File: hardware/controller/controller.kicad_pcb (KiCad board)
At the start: 2 copper layers, 47 parts, among them J1 Conn_01x02_Pin, J11 Barrel_Jack, J12 USB_C_Receptacle_USB2.0_14P, J2 Conn_01x02_Pin, J3 Conn_01x02_Pin, J5 Screw_Terminal_01x02, J6 Screw_Terminal_01x02, J7 Conn_01x04_Pin, J8 Conn_01x04_Pin, U1 ESP32-C3-MINI-1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

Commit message: First stab at board routing
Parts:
- removed C9: 0.1uf, Capacitor_SMD:C_0805_2012Metric
- removed the R4 at (155.4, 96.5)
- J6: moved to F.Cu
- TP1, TP2, TP3, TP4, TP5: footprint TestPoint:TestPoint_Pad_D2.0mm -> TestPoint:TestPoint_THTPad_2.0x2.0mm_Drill1.0mm
- moved TP1 42.5 mm to (121.3, 113.0)
- moved TP2 41.1 mm to (117.5, 113.0)
- moved TP3 40.4 mm to (113.7, 113.0)
- moved R2 23.4 mm to (129.8, 75.6), turned to 90 degrees
- moved R11 22.8 mm to (129.8, 79.4), turned to -90 degrees
- moved R9 18.4 mm to (121.9, 96.3), turned to -90 degrees
- moved TP4 16.5 mm to (158.1, 77.9)
- moved TP5 16.5 mm to (158.1, 81.9)
- moved C2 15.6 mm to (122.6, 104.5), turned to -90 degrees
- moved U8 15.3 mm to (118.5, 92.7)
- moved C8 15.1 mm to (113.5, 74.6), turned to 90 degrees
- moved U9 15.1 mm to (118.5, 96.3)
- moved D2 14.9 mm to (160.2, 104.6)
- moved R8 14.6 mm to (121.9, 92.7), turned to -90 degrees
- moved R3 14.2 mm to (160.1, 106.9)
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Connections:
- U1 pad 18: SCK -> CS0
- U1 pad 19: CS0 -> SCK
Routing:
- net GND: track 0.00 -> 95.5 mm, vias 0 -> 43
- net /Microcontroller/HEATER: track 0.00 -> 82.3 mm, vias 0 -> 2
- net +12V: track 0.00 -> 75.5 mm, vias 0 -> 1
- net SO: track 0.00 -> 49.9 mm
- net SCK: track 0.00 -> 47.5 mm, vias 0 -> 3
- net VBUS: track 0.00 -> 39.3 mm, vias 0 -> 2
- net FAN_1_TACH: track 0.00 -> 36.3 mm
- net FAN_0_TACH: track 0.00 -> 33.3 mm
- net CS2: track 0.00 -> 32.4 mm
- net +3V3: track 0.00 -> 28.7 mm, vias 0 -> 10
- net /Microcontroller/USB_D+: track 0.00 -> 28.0 mm, vias 0 -> 2
- net /Microcontroller/LED: track 0.00 -> 26.7 mm, vias 0 -> 2
- net CS1: track 0.00 -> 26.1 mm
- net CS0: track 0.00 -> 25.8 mm
- net /Microcontroller/USB_D-: track 0.00 -> 25.7 mm, vias 0 -> 2
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- added copper zone on In2.Cu, net +3V3
- added copper zone on F.Cu, net GND
- added copper zone on In1.Cu, net GND
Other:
- board outline added: 57.9 x 45.2 mm
- copper layers 2 -> 4
- board text added: "Andrew Reilley v1"
- board text added: "EZ-Bake"

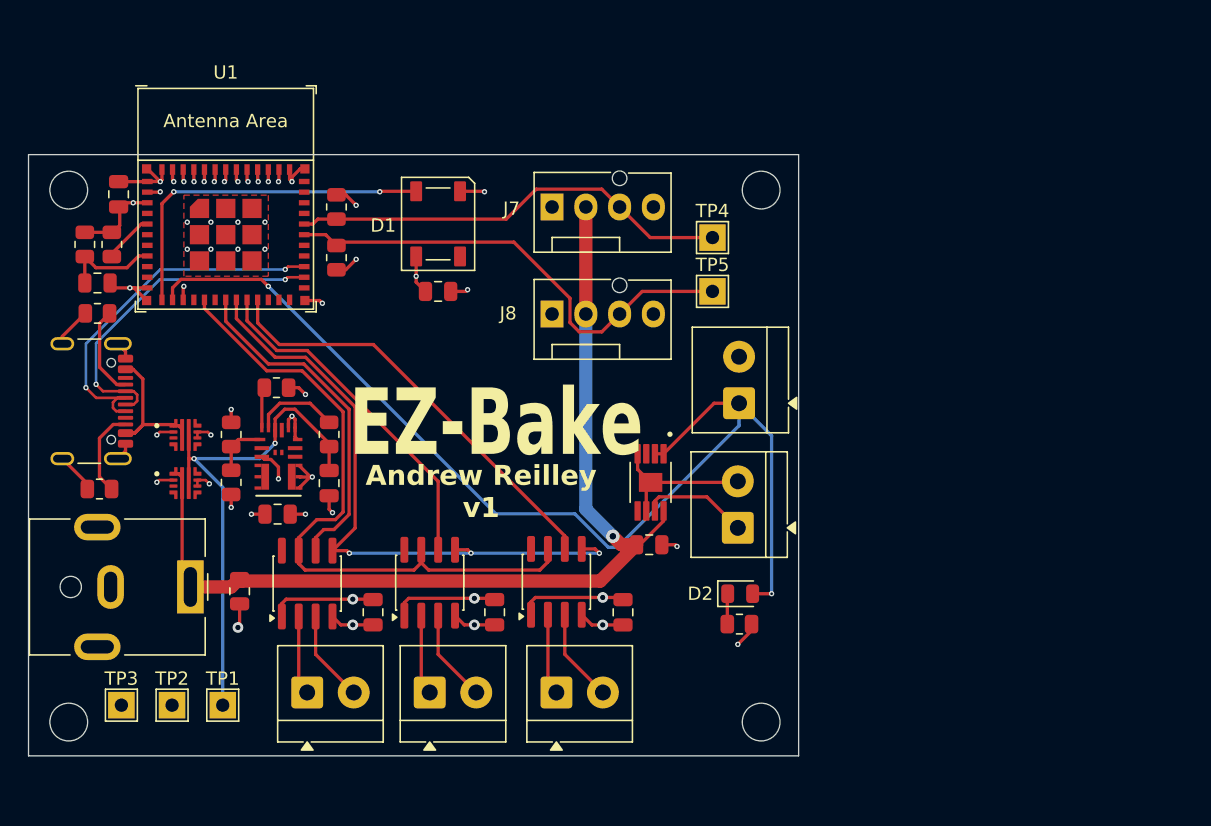
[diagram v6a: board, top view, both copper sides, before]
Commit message: Layout tweaks
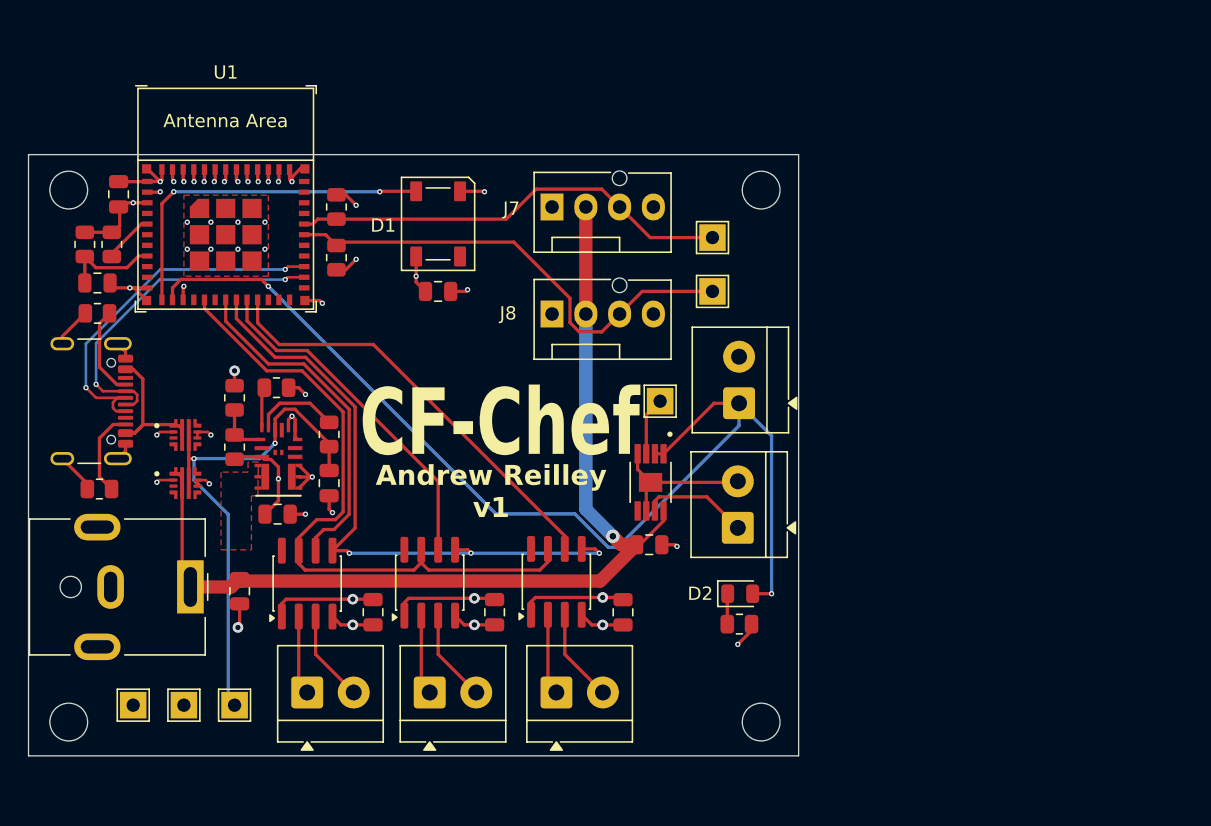
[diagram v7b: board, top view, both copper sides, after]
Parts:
- added TP6: TestPoint, TestPoint:TestPoint_THTPad_2.0x2.0mm_Drill1.0mm, F.Cu at (154.2, 90.2)
- moved R8 2.77 mm to (122.2, 89.9)
- moved R9 2.67 mm to (122.2, 93.6)
- moved TP1 0.89 mm to (122.2, 113.0)
- moved TP2 0.89 mm to (118.4, 113.0)
- moved TP3 0.89 mm to (114.6, 113.0)
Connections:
- U6 pad 3: unconnected-(U6-~{FAULT}-Pad3) -> Net-(U6-~{FAULT})
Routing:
- net Net-(U6-~{FAULT}): track 0.00 -> 4.39 mm
- net GND: track 95.5 -> 98.7 mm, vias 43 -> 41
- added copper zone on F.Cu, net /Power/V_SW
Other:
- board text added: "${REFERENCE}"
- board text added: "CF-Chef"
- board text removed: "EZ-Bake"

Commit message: Rounded corners, fixed up labels
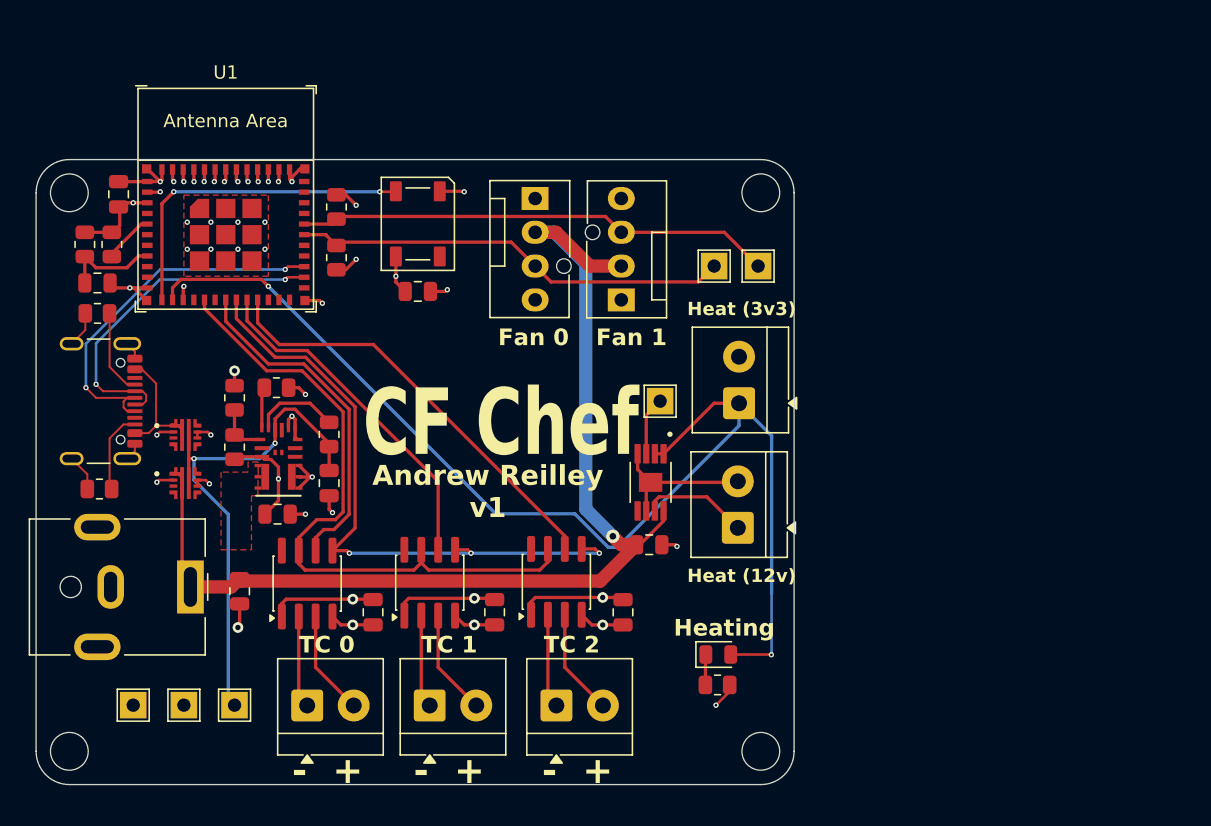
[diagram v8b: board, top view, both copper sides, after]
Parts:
- Fan 0: renamed from J7
- Fan 1: renamed from J8
- moved Fan 1 5.32 mm to (151.3, 82.5), turned to 90 degrees
- moved Heating 4.86 mm to (158.6, 109.2)
- moved R3 4.86 mm to (158.5, 111.5)
- moved TP4 4.04 mm to (161.5, 80.0)
- moved TP5 1.91 mm to (158.2, 80.0)
- moved C12 1.52 mm to (136.0, 81.9)
- moved D1 1.52 mm to (136.0, 76.8)
- moved Fan 0 1.42 mm to (144.8, 74.9), turned to -90 degrees
- moved J1 0.98 mm to (127.6, 113.1)
- moved J2 0.98 mm to (136.8, 113.1)
- moved J3 0.98 mm to (146.4, 113.1)
- moved J12 0.70 mm to (111.0, 90.2)
- renumbered D2 to Heating
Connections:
- R11 pad 1: FAN_1_TACH -> FAN_0_TACH
- R2 pad 1: FAN_0_TACH -> FAN_1_TACH
- TP4 pad 1: FAN_0_TACH -> FAN_1_TACH
- TP5 pad 1: FAN_1_TACH -> FAN_0_TACH
- U1 pad 30: FAN_1_TACH -> FAN_0_TACH
- U1 pad 31: FAN_0_TACH -> FAN_1_TACH
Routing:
- net +12V: track 75.5 -> 83.5 mm
- net /Microcontroller/HEATER: track 82.3 -> 88.5 mm
- net +5V: track 11.7 -> 9.65 mm
- net /Microcontroller/LED: track 26.7 -> 25.3 mm
- net Net-(J3-Pin_2): track 7.03 -> 8.01 mm
- net Net-(J3-Pin_1): track 6.11 -> 7.08 mm
- net Net-(J2-Pin_2): track 6.97 -> 7.94 mm
- net Net-(J2-Pin_1): track 6.04 -> 7.02 mm
- net Net-(J1-Pin_2): track 6.90 -> 7.88 mm
- net Net-(J1-Pin_1): track 5.98 -> 6.95 mm
- net GND: track 98.7 -> 97.9 mm
- net /Microcontroller/USB_D-: track 25.7 -> 26.3 mm
- net /Microcontroller/USB_D+: track 28.0 -> 28.5 mm
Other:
- board size 57.9 x 45.2 mm -> 57 x 47 mm
- board text added: "- +"
- board text added: "CF Chef"
- board text added: "Fan 0"
- board text added: "Fan 1"
- board text added: "Heat (12v)"
- board text added: "Heat (3v3)"
- board text added: "Heating"
- board text added: "TC 0"
- board text added: "TC 1"
- board text added: "TC 2"
- board text removed: "CF-Chef"
